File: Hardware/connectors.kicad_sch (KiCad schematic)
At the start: 52 parts, among them J10 CAN BUS, J11 CAN BUS, J2 FPV, J3 ST_LINK, J4 GPS, J5 Airspeed sensor, J6 4in1 ESC, J7 RC Receiver, J8 VTX, J9 DJI

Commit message: /HARDWARE: Updated BOM do not Include list
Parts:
- TP1, TP10, TP12, TP13, TP14, TP15, TP16, TP17, TP18, TP2, TP20, TP21, TP22, TP23, TP24, TP25, TP26, TP27, TP28, TP29, TP3, TP30, TP31, TP32, TP33, TP34, TP35, TP36, TP37, TP38, TP39, TP4, TP40, TP41, TP42, TP43, TP45, TP5, TP6, TP7, TP8, TP9: now left out of the parts list
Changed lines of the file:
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@@
 		(body_style 1)
 		(exclude_from_sim no)
-		(in_bom yes)
+		(in_bom no)
 		(on_board yes)
 		(in_pos_files yes)
@@
 		(body_style 1)
 		(exclude_from_sim no)
-		(in_bom yes)
+		(in_bom no)
 		(on_board yes)
 		(in_pos_files yes)
@@
 		(body_style 1)
 		(exclude_from_sim no)
-		(in_bom yes)
+		(in_bom no)
 		(on_board yes)
 		(in_pos_files yes)
@@
 		(body_style 1)
 		(exclude_from_sim no)
-		(in_bom yes)
+		(in_bom no)
 		(on_board yes)
 		(in_pos_files yes)
@@
 		(body_style 1)
 		(exclude_from_sim no)
-		(in_bom yes)
+		(in_bom no)
 		(on_board yes)
 		(in_pos_files yes)
@@
 		(body_style 1)
 		(exclude_from_sim no)
-		(in_bom yes)
+		(in_bom no)
 		(on_board yes)
 		(in_pos_files yes)
@@
 		(body_style 1)
 		(exclude_from_sim no)
-		(in_bom yes)
+		(in_bom no)
 		(on_board yes)
 		(in_pos_files yes)
@@
 		(body_style 1)
 		(exclude_from_sim no)
-		(in_bom yes)
+		(in_bom no)
 		(on_board yes)
 		(in_pos_files yes)
@@
 		(body_style 1)
 		(exclude_from_sim no)
-		(in_bom yes)
+		(in_bom no)
 		(on_board yes)
 		(in_pos_files yes)
@@
 		(body_style 1)
 		(exclude_from_sim no)
-		(in_bom yes)
+		(in_bom no)
 		(on_board yes)
 		(in_pos_files yes)
@@
 		(body_style 1)
 		(exclude_from_sim no)
-		(in_bom yes)
+		(in_bom no)
 		(on_board yes)
 		(in_pos_files yes)
@@
 		(body_style 1)
 		(exclude_from_sim no)
-		(in_bom yes)
+		(in_bom no)
 		(on_board yes)
 		(in_pos_files yes)
@@
 		(body_style 1)
 		(exclude_from_sim no)
-		(in_bom yes)
+		(in_bom no)
 		(on_board yes)
 		(in_pos_files yes)
@@
 		(body_style 1)
 		(exclude_from_sim no)
-		(in_bom yes)
+		(in_bom no)
 		(on_board yes)
 		(in_pos_files yes)
@@
 		(body_style 1)
 		(exclude_from_sim no)
-		(in_bom yes)
+		(in_bom no)
 		(on_board yes)
 		(in_pos_files yes)
@@
 		(body_style 1)
 		(exclude_from_sim no)
-		(in_bom yes)
+		(in_bom no)
 		(on_board yes)
 		(in_pos_files yes)
@@
 		(body_style 1)
 		(exclude_from_sim no)
-		(in_bom yes)
+		(in_bom no)
 		(on_board yes)
 		(in_pos_files yes)
@@
 		(body_style 1)
 		(exclude_from_sim no)
-		(in_bom yes)
+		(in_bom no)
 		(on_board yes)
 		(in_pos_files yes)
@@
 		(body_style 1)
 		(exclude_from_sim no)
-		(in_bom yes)
+		(in_bom no)
 		(on_board yes)
 		(in_pos_files yes)
@@
 		(body_style 1)
 		(exclude_from_sim no)
-		(in_bom yes)
+		(in_bom no)
 		(on_board yes)
 		(in_pos_files yes)
@@
 		(body_style 1)
 		(exclude_from_sim no)
-		(in_bom yes)
+		(in_bom no)
 		(on_board yes)
 		(in_pos_files yes)
@@
 		(body_style 1)
 		(exclude_from_sim no)
-		(in_bom yes)
+		(in_bom no)
 		(on_board yes)
 		(in_pos_files yes)
@@
 		(body_style 1)
 		(exclude_from_sim no)
-		(in_bom yes)
+		(in_bom no)
 		(on_board yes)
 		(in_pos_files yes)
@@
 		(body_style 1)
 		(exclude_from_sim no)
-		(in_bom yes)
+		(in_bom no)
 		(on_board yes)
 		(in_pos_files yes)
@@
 		(body_style 1)
 		(exclude_from_sim no)
-		(in_bom yes)
+		(in_bom no)
 		(on_board yes)
 		(in_pos_files yes)
@@
 		(body_style 1)
 		(exclude_from_sim no)
-		(in_bom yes)
+		(in_bom no)
 		(on_board yes)
 		(in_pos_files yes)
@@
 		(body_style 1)
 		(exclude_from_sim no)
-		(in_bom yes)
+		(in_bom no)
 		(on_board yes)
 		(in_pos_files yes)
@@
 		(body_style 1)
 		(exclude_from_sim no)
-		(in_bom yes)
+		(in_bom no)
 		(on_board yes)
 		(in_pos_files yes)
@@
 		(body_style 1)
 		(exclude_from_sim no)
-		(in_bom yes)
+		(in_bom no)
 		(on_board yes)
 		(in_pos_files yes)
@@
 		(body_style 1)
 		(exclude_from_sim no)
-		(in_bom yes)
+		(in_bom no)
 		(on_board yes)
 		(in_pos_files yes)
@@
 		(body_style 1)
 		(exclude_from_sim no)
-		(in_bom yes)
+		(in_bom no)
 		(on_board yes)
 		(in_pos_files yes)
@@
 		(body_style 1)
 		(exclude_from_sim no)
-		(in_bom yes)
+		(in_bom no)
 		(on_board yes)
 		(in_pos_files yes)
@@
 		(body_style 1)
 		(exclude_from_sim no)
-		(in_bom yes)
+		(in_bom no)
 		(on_board yes)
 		(in_pos_files yes)
@@
 		(body_style 1)
 		(exclude_from_sim no)
-		(in_bom yes)
+		(in_bom no)
 		(on_board yes)
 		(in_pos_files yes)
@@
 		(body_style 1)
 		(exclude_from_sim no)
-		(in_bom yes)
+		(in_bom no)
 		(on_board yes)
 		(in_pos_files yes)
@@
 		(body_style 1)
 		(exclude_from_sim no)
-		(in_bom yes)
+		(in_bom no)
 		(on_board yes)
 		(in_pos_files yes)
@@
 		(body_style 1)
 		(exclude_from_sim no)
-		(in_bom yes)
+		(in_bom no)
 		(on_board yes)
 		(in_pos_files yes)
@@
 		(body_style 1)
 		(exclude_from_sim no)
-		(in_bom yes)
+		(in_bom no)
 		(on_board yes)
 		(in_pos_files yes)
@@
 		(body_style 1)
 		(exclude_from_sim no)
-		(in_bom yes)
+		(in_bom no)
 		(on_board yes)
 		(in_pos_files yes)
@@
 		(body_style 1)
 		(exclude_from_sim no)
-		(in_bom yes)
+		(in_bom no)
 		(on_board yes)
 		(in_pos_files yes)
@@
 		(body_style 1)
 		(exclude_from_sim no)
-		(in_bom yes)
+		(in_bom no)
 		(on_board yes)
 		(in_pos_files yes)
@@
 		(body_style 1)
 		(exclude_from_sim no)
-		(in_bom yes)
+		(in_bom no)
 		(on_board yes)
 		(in_pos_files yes)

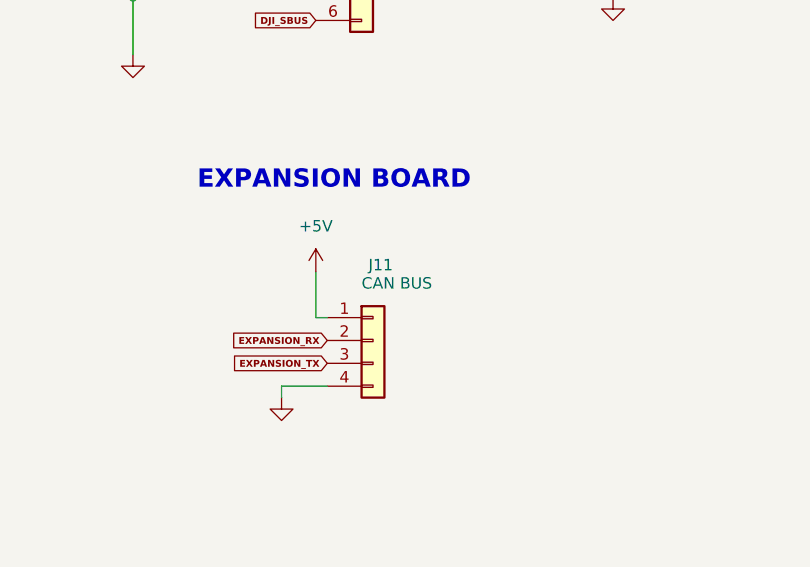
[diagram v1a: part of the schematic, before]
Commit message: /HARDWARE: corrected schematics naming
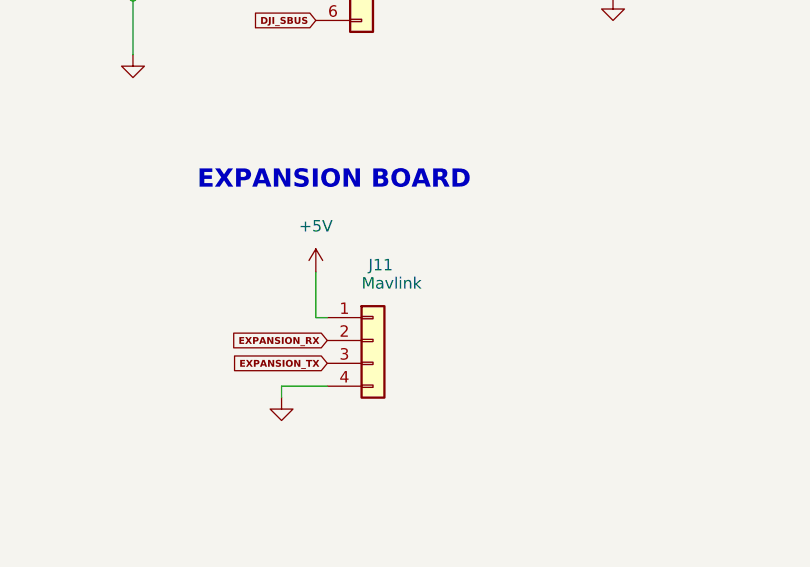
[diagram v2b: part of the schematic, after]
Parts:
- J11: value CAN BUS -> Mavlink
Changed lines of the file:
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@@
 			)
 		)
-		(property "Value" "CAN BUS"
+		(property "Value" "Mavlink"
 			(at 262.89 184.15 0)
 			(show_name no)
